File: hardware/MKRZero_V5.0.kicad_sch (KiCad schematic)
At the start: 55 parts, among them IC1 PCF8523T, IC2 CR1220-2, J1 USB_B_Micro, J2 2X3_SMD_MALE, J3 AMPHENOL_114-00841-68, J6 Conn_01x08_Pin, J7 Conn_01x04_Pin, J8 PJ-320A, Q1 32.768KHz, SW1 RotaryEncoder_Switch_MP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

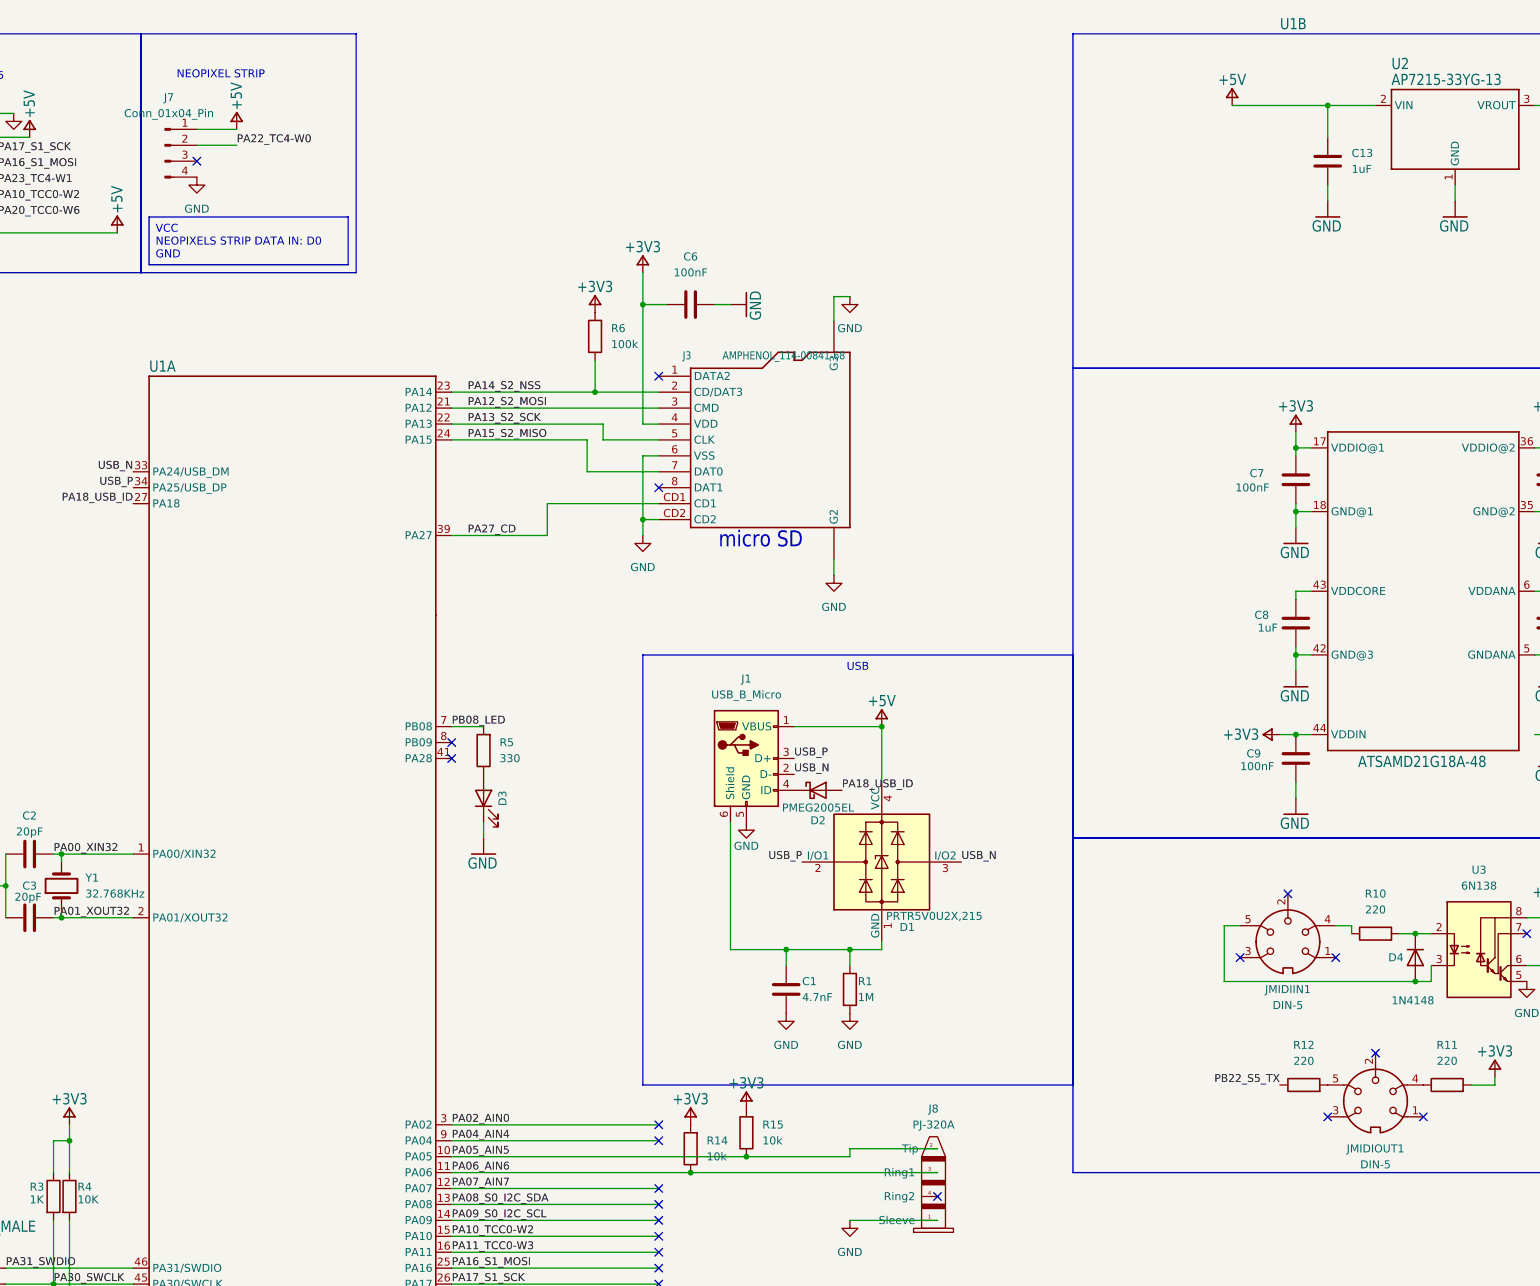
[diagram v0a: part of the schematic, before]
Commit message: midi connector corrections, use MG03254F-RA magnetic pogo 3pin connector
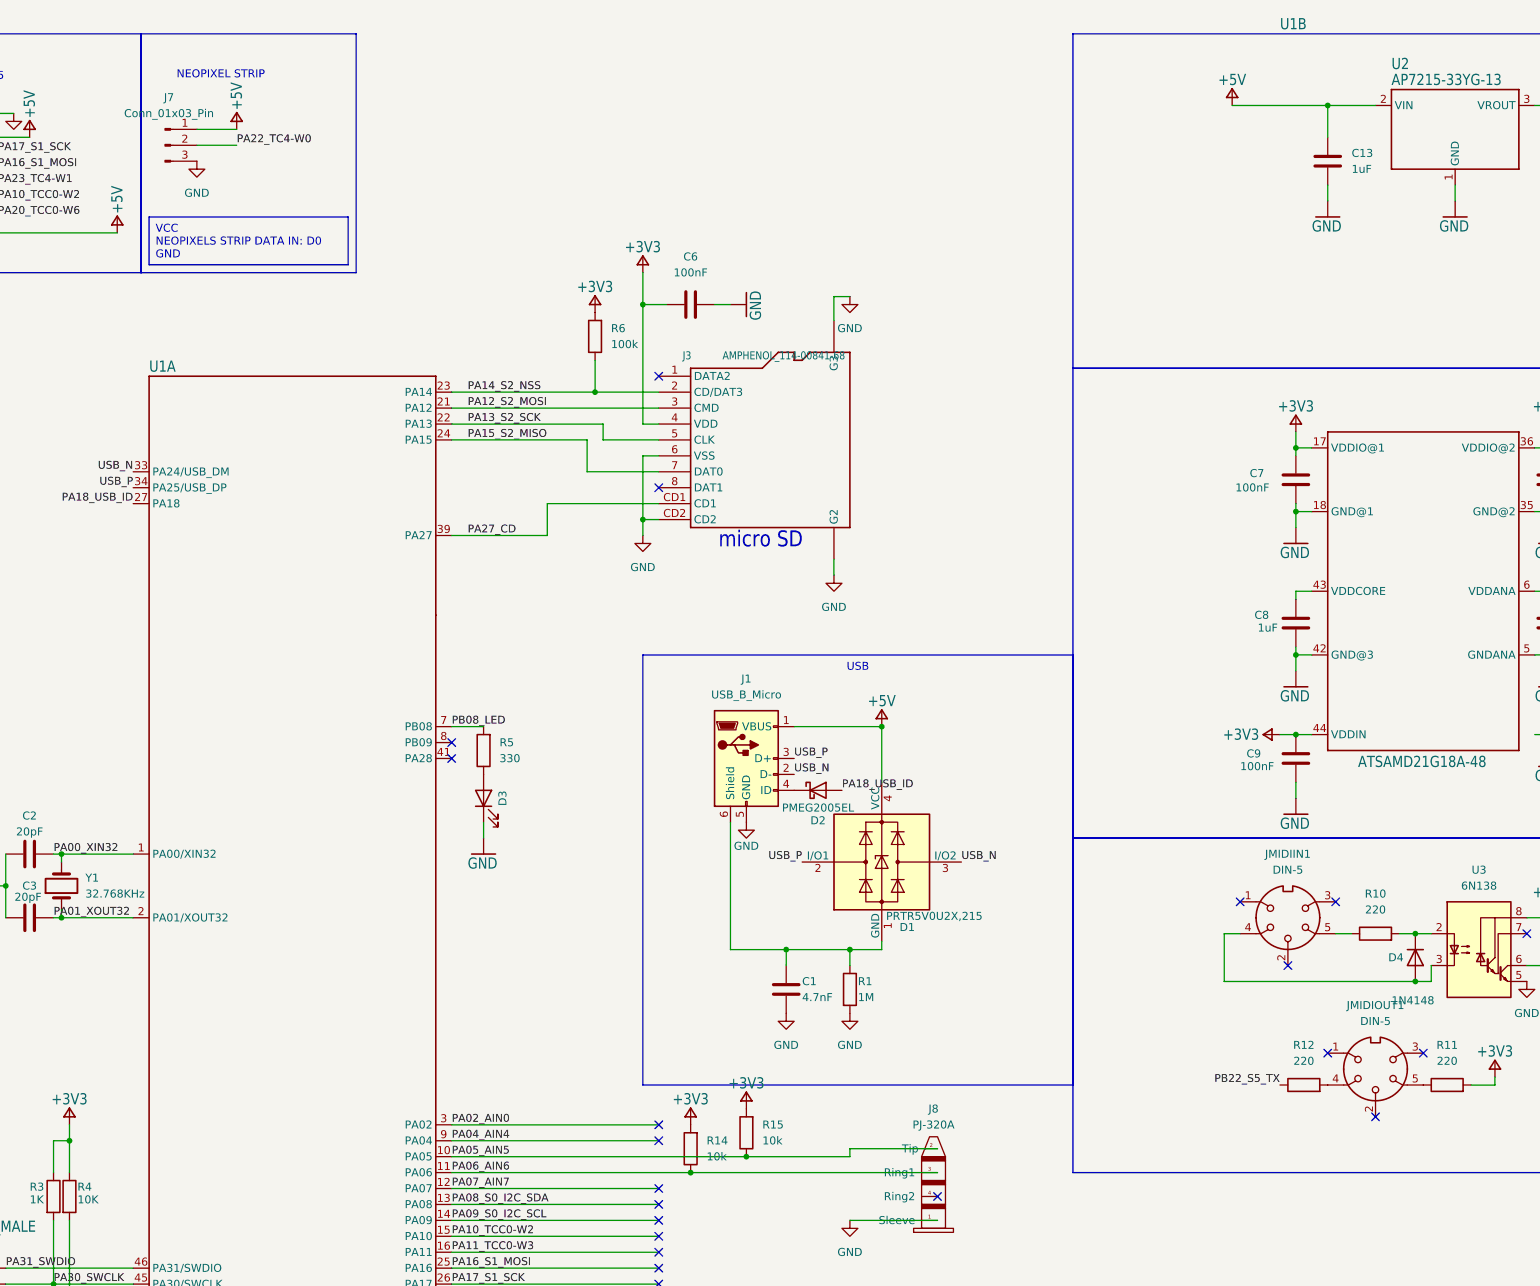
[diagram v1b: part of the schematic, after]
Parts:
- removed J7: Conn_01x04_Pin, Connector_JST:JST_SH_SM04B-SRSS-TB_1x04-1MP_P1.00mm_Horizontal, symbol Connector:Conn_01x04_Pin
- added J7: Conn_01x03_Pin, MKRZero_V5.0:MG03254F-RA, symbol Connector:Conn_01x03_Pin
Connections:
- net +5V: now also J7.1 (Pin_1)
- net GND: now also J7.3 (Pin_3)
- net PA22_TC4-W0: now also J7.2 (Pin_2)
- net at D4.2 (A), U3.3 (C2): now also JMIDIIN1.4; no longer JMIDIIN1.5
- net at JMIDIOUT1.4: now also R12.2; no longer R11.1
- net at JMIDIOUT1.5: now also R11.1; no longer R12.2
- net at R10.1: now also JMIDIIN1.5; no longer JMIDIIN1.4
- no-connect marks 64 -> 63
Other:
- moved on the sheet: JMIDIIN1, JMIDIOUT1
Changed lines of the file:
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@@
 	)
 	(no_connect
-		(at 250.19 172.72)
+		(at 250.19 162.56)
 	)
 	(no_connect
@@
 	)
 	(no_connect
-		(at 242.57 162.56)
+		(at 242.57 172.72)
 	)
 	(no_connect
@@
 	)
 	(no_connect
-		(at 54.61 20.32)
-	)
-	(no_connect
 		(at 128.27 212.09)
 	)
@@
 	)
 	(no_connect
-		(at 234.95 172.72)
+		(at 234.95 162.56)
 	)
 	(no_connect
@@
 	)
 	(no_connect
-		(at 236.22 147.32)
+		(at 236.22 138.43)
 	)
 	(no_connect
@@
 	)
 	(no_connect
-		(at 228.6 137.16)
+		(at 220.98 138.43)
 	)
 	(no_connect
@@
 	)
 	(no_connect
-		(at 220.98 147.32)
+		(at 228.6 148.59)
 	)
 	(no_connect
@@
 	(wire
 		(pts
-			(xy 236.22 142.24) (xy 238.76 142.24)
+			(xy 236.22 143.51) (xy 238.76 143.51)
 		)
 		(stroke
@@
 	(wire
 		(pts
-			(xy 218.44 142.24) (xy 220.98 142.24)
+			(xy 218.44 143.51) (xy 220.98 143.51)
 		)
 		(stroke
@@
 	(wire
 		(pts
-			(xy 218.44 151.13) (xy 218.44 142.24)
+			(xy 218.44 151.13) (xy 218.44 143.51)
 		)
 		(stroke
@@
 	(wire
 		(pts
-			(xy 238.76 142.24) (xy 238.76 143.51)
-		)
-		(stroke
-			(width 0)
-			(type default)
-		)
-	)
-	(wire
-		(pts
 			(xy 128.27 217.17) (xy 95.25 217.17)
 		)
@@
 	)
 	(symbol
+		(lib_id "Connector:Conn_01x03_Pin")
+		(at 49.53 17.78 0)
+		(unit 1)
+		(exclude_from_sim no)
+		(in_bom yes)
+		(on_board yes)
+		(dnp no)
+		(fields_autoplaced yes)
+		(property "Reference" "J7"
+			(at 50.165 10.16 0)
+			(effects
+				(font
+					(size 1.27 1.27)
+				)
+			)
+		)
+		(property "Value" "Conn_01x03_Pin"
+			(at 50.165 12.7 0)
+			(effects
+				(font
+					(size 1.27 1.27)
+				)
+			)
+		)
+		(property "Footprint" "MKRZero_V5.0:MG03254F-RA"
+			(at 49.53 17.78 0)
+			(effects
+				(font
+					(size 1.27 1.27)
+				)
+				(hide yes)
+			)
+		)
+		(property "Datasheet" "~"
+			(at 49.53 17.78 0)
+			(effects
+				(font
+					(size 1.27 1.27)
+				)
+				(hide yes)
+			)
+		)
+		(property "Description" "Generic connector, single row, 01x03, script generated"
+			(at 49.53 17.78 0)
+			(effects
+				(font
+					(size 1.27 1.27)
+				)
+				(hide yes)
+			)
+		)
+		(pin "3"
+		)
+		(pin "1"
+		)
+		(pin "2"
+		)
+		(instances
+			(project ""
+				(path "/d69da2de-79eb-4848-90e3-5c89e1fd8e2f"
+					(reference "J7")
+					(unit 1)
+				)
+			)
+		)
+	)
+	(symbol
 		(lib_id "power:GND")
-		(at 54.61 22.86 0)
+		(at 54.61 20.32 0)
 		(unit 1)
 		(exclude_from_sim no)
@@
 		(fields_autoplaced yes)
 		(property "Reference" "#PWR08"
-			(at 54.61 29.21 0)
+			(at 54.61 26.67 0)
 			(effects
 				(font
@@
 		)
 		(property "Value" "GND"
-			(at 54.61 27.94 0)
+			(at 54.61 25.4 0)
 			(effects
 				(font
@@
 		)
 		(property "Footprint" ""
-			(at 54.61 22.86 0)
+			(at 54.61 20.32 0)
 			(effects
 				(font
@@
 		)
 		(property "Datasheet" ""
-			(at 54.61 22.86 0)
+			(at 54.61 20.32 0)
 			(effects
 				(font
@@
 		)
 		(property "Description" "Power symbol creates a global label with name \"GND\" , ground"
-			(at 54.61 22.86 0)
+			(at 54.61 20.32 0)
 			(effects
 				(font
@@
 		(lib_name "DIN-5_1")
 		(lib_id "Connector:DIN-5")
-		(at 242.57 170.18 0)
+		(at 242.57 165.1 180)
 		(unit 1)
 		(exclude_from_sim no)
@@
 		(fields_autoplaced yes)
 		(property "Reference" "JMIDIOUT1"
-			(at 242.5701 177.8 0)
+			(at 242.5699 154.94 0)
 			(effects
 				(font
@@
 		)
 		(property "Value" "DIN-5"
-			(at 242.5701 180.34 0)
+			(at 242.5699 157.48 0)
 			(effects
 				(font
@@
 		)
 		(property "Footprint" "MKRZero_V5.0:Deltron-671-0501-5"
-			(at 242.57 170.18 0)
+			(at 242.57 165.1 0)
 			(effects
 				(font
@@
 		)
 		(property "Datasheet" "http://www.mouser.com/ds/2/18/40_c091_abd_e-75918.pdf"
-			(at 242.57 170.18 0)
+			(at 242.57 165.1 0)
 			(effects
 				(font
@@
 		)
 		(property "Description" "5-pin DIN connector"
-			(at 242.57 170.18 0)
+			(at 242.57 165.1 0)
 			(effects
 				(font
@@
 		)
 		(property "LCSC" "C20611696"
-			(at 242.5701 177.8 0)
+			(at 242.5699 157.48 0)
 			(effects
 				(font
@@
 	)
 	(symbol
-		(lib_id "Connector:Conn_01x04_Pin")
-		(at 49.53 17.78 0)
-		(unit 1)
-		(exclude_from_sim no)
-		(in_bom yes)
-		(on_board yes)
-		(dnp no)
-		(fields_autoplaced yes)
-		(property "Reference" "J7"
-			(at 50.165 10.16 0)
-			(effects
-				(font
-					(size 1.27 1.27)
-				)
-			)
-		)
-		(property "Value" "Conn_01x04_Pin"
-			(at 50.165 12.7 0)
-			(effects
-				(font
-					(size 1.27 1.27)
-				)
-			)
-		)
-		(property "Footprint" "Connector_JST:JST_SH_SM04B-SRSS-TB_1x04-1MP_P1.00mm_Horizontal"
-			(at 49.53 17.78 0)
-			(effects
-				(font
-					(size 1.27 1.27)
-				)
-				(hide yes)
-			)
-		)
-		(property "Datasheet" "~"
-			(at 49.53 17.78 0)
-			(effects
-				(font
-					(size 1.27 1.27)
-				)
-				(hide yes)
-			)
-		)
-		(property "Description" "Generic connector, single row, 01x04, script generated"
-			(at 49.53 17.78 0)
-			(effects
-				(font
-					(size 1.27 1.27)
-				)
-				(hide yes)
-			)
-		)
-		(property "LCSC" "C462077"
-			(at 50.165 10.16 0)
-			(effects
-				(font
-					(size 1.27 1.27)
-				)
-				(hide yes)
-			)
-		)
-		(pin "1"
-		)
-		(pin "2"
-		)
-		(pin "3"
-		)
-		(pin "4"
-		)
-		(instances
-			(project ""
-				(path "/d69da2de-79eb-4848-90e3-5c89e1fd8e2f"
-					(reference "J7")
-					(unit 1)
-				)
-			)
-		)
-	)
-	(symbol
 		(lib_id "MKRZero_V5.0-eagle-import:+3V3")
 		(at 261.62 163.83 0)
@@
 		(lib_name "DIN-5_1")
 		(lib_id "Connector:DIN-5")
-		(at 228.6 144.78 0)
+		(at 228.6 140.97 180)
 		(unit 1)
 		(exclude_from_sim no)
@@
 		(fields_autoplaced yes)
 		(property "Reference" "JMIDIIN1"
-			(at 228.6001 152.4 0)
+			(at 228.5999 130.81 0)
 			(effects
 				(font
@@
 		)
 		(property "Value" "DIN-5"
-			(at 228.6001 154.94 0)
+			(at 228.5999 133.35 0)
 			(effects
 				(font
@@
 		)
 		(property "Footprint" "MKRZero_V5.0:Deltron-671-0501-5"
-			(at 228.6 144.78 0)
+			(at 228.6 140.97 0)
 			(effects
 				(font
@@
 		)
 		(property "Datasheet" "http://www.mouser.com/ds/2/18/40_c091_abd_e-75918.pdf"
-			(at 228.6 144.78 0)
+			(at 228.6 140.97 0)
 			(effects
 				(font
@@
 		)
 		(property "Description" "5-pin DIN connector"
-			(at 228.6 144.78 0)
+			(at 228.6 140.97 0)
 			(effects
 				(font
@@
 		)
 		(property "LCSC" "C20611696"
-			(at 228.6001 152.4 0)
+			(at 228.5999 133.35 0)
 			(effects
 				(font

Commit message: midi still not working
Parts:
- added C15: .1uF, Capacitor_SMD:C_0805_2012Metric, symbol Device:C
- added U4: W25Q128JVS, Package_SO:SOIC-8W_5.3x5.3mm_P1.27mm, symbol Memory_Flash:W25Q128JVS
- J2: LCSC C124390 -> C3294461
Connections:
- net +3V3: now also C15.2, U4.3 (IO2), U4.7 (IO3), U4.8 (VCC)
- net GND: now also C15.1, U4.4 (GND)
- net PA04_AIN4: now also SW1.B
- net PA16_S1_MOSI: now also U4.5 (DI(IO0))
- net PA17_S1_SCK: now also U4.6 (CLK)
- net PA19_S1_MISO: now also U4.2 (DO(IO1)); no longer SW1.B
- net PB03_AIN11: now also U4.1 (~{CS})
- no-connect marks 63 -> 61
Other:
- note removed: "RESET"
- moved on the sheet: C4, C5, IC1, IC2, Q1, R13, R7, R8

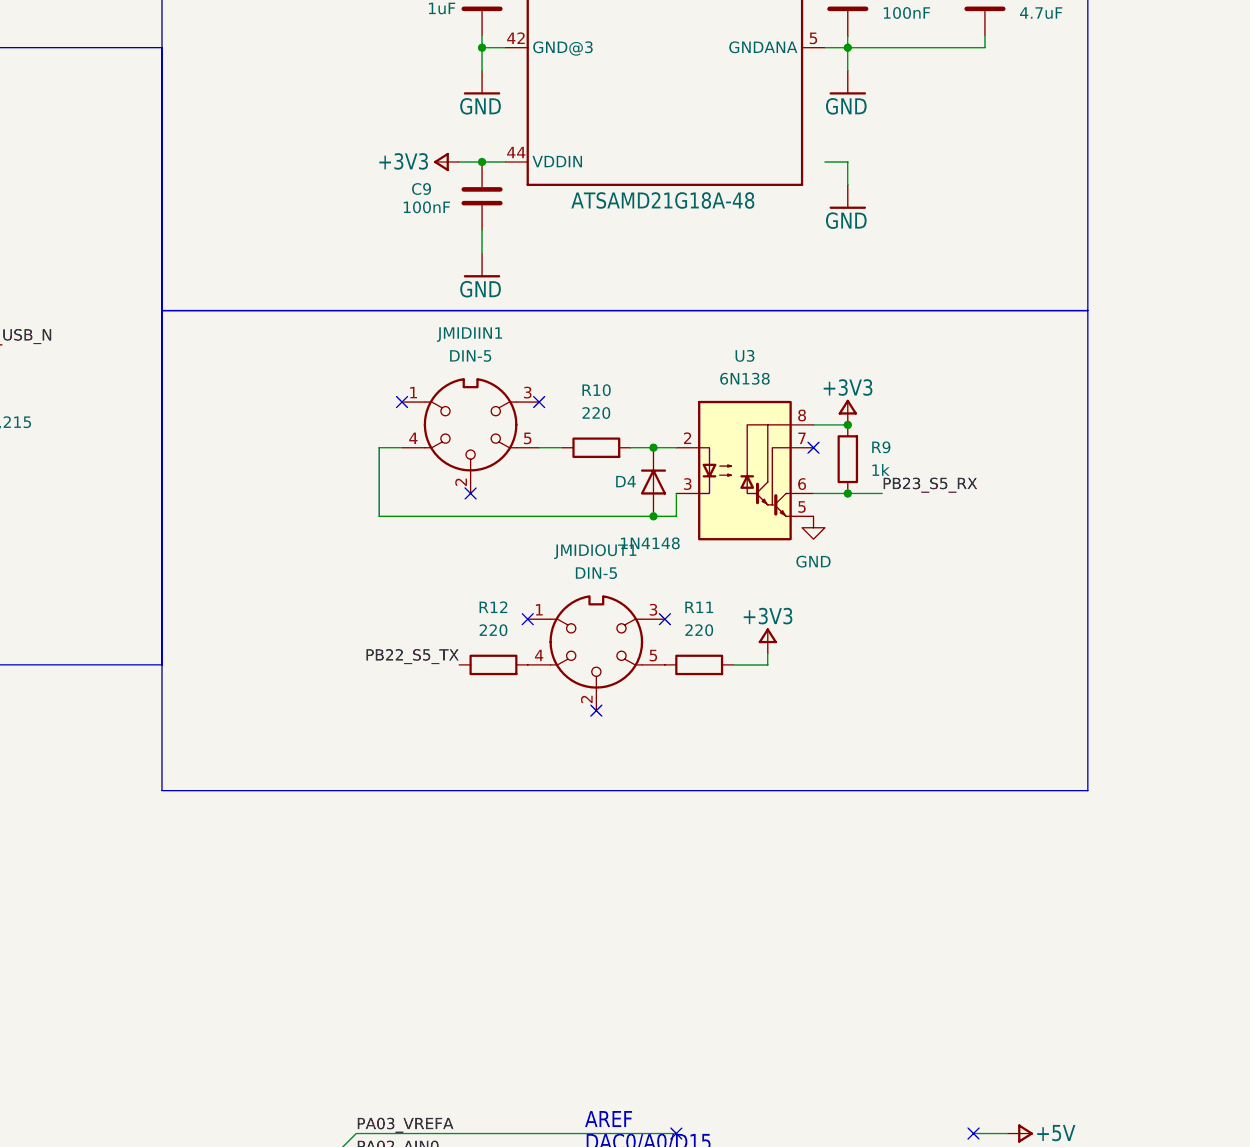
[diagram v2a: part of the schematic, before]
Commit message: v1.3 hopefully midi in will work this time?
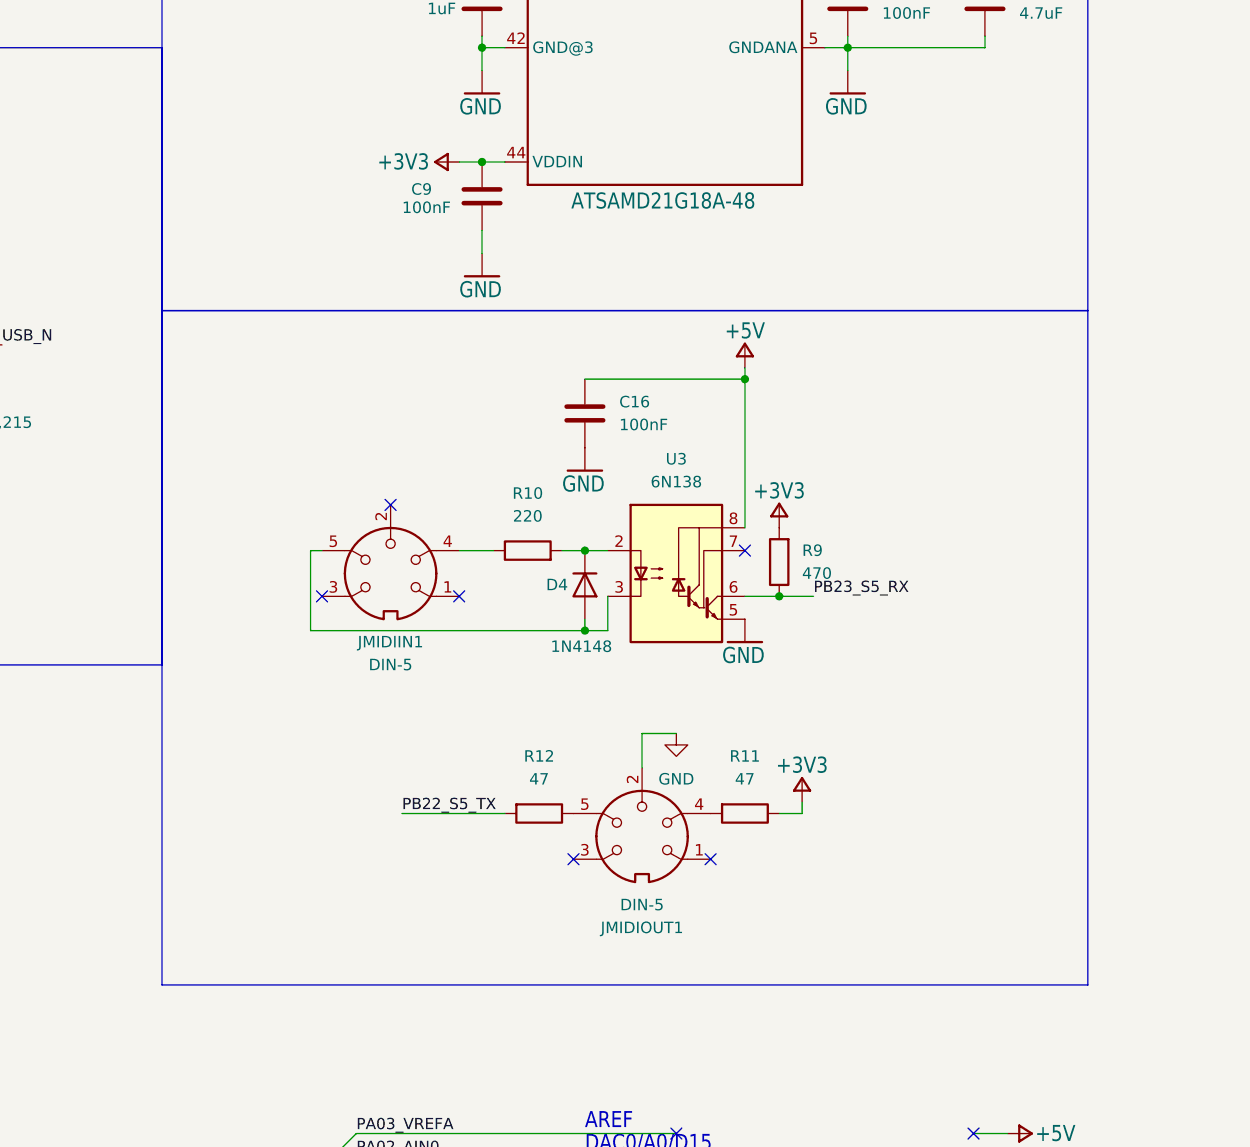
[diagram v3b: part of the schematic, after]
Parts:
- added C16: 100nF, Capacitor_SMD:C_0402_1005Metric, symbol Device:C
- R11, R12: value 220 -> 47; footprint Resistor_SMD:R_0402_1005Metric -> Resistor_SMD:R_0805_2012Metric; LCSC C25091 -> C17714
- R9: value 1k -> 470; footprint Resistor_SMD:R_0402_1005Metric -> Resistor_SMD:R_0805_2012Metric; LCSC C11702 -> C17710
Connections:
- net +3V3: now also R11.1; no longer R11.2, U3.8 (VCC)
- net +5V: now also U3.8 (VCC), C16.2
- net GND: now also JMIDIOUT1.2, C16.1
- net PB22_S5_TX: now also R12.2; no longer R12.1
- net at D4.2 (A), U3.3 (C2): now also JMIDIIN1.5; no longer JMIDIIN1.4
- net at JMIDIOUT1.4: now also R11.2; no longer R12.2
- net at JMIDIOUT1.5: now also R12.1; no longer R11.1
- net at R10.1: now also JMIDIIN1.4; no longer JMIDIIN1.5
- no-connect marks 61 -> 60
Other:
- moved on the sheet: D4, JMIDIIN1, JMIDIOUT1, R10, R11, R12, R9, U3
